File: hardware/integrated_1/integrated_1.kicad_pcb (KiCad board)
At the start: 2 copper layers, 37 parts, among them J1 USB4105-GF-A-120, U1 XC6SLX9-TQG144, U2 MAX17620ATA, U5 RP2040

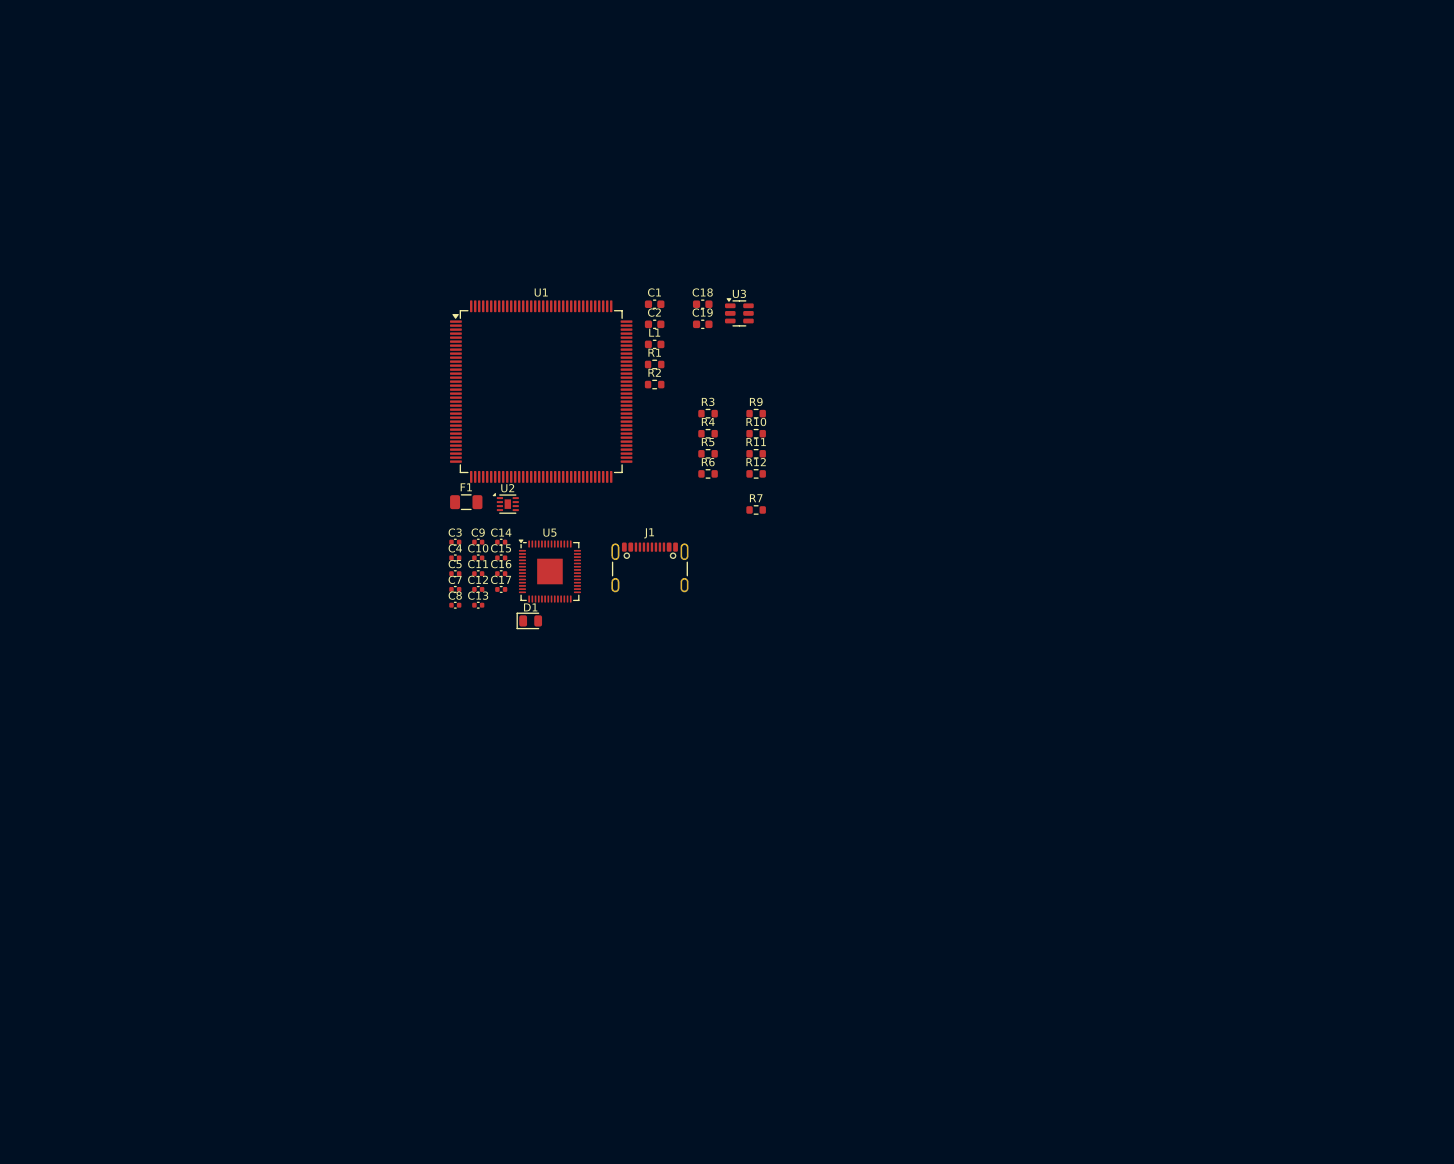
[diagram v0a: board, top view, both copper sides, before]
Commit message: created a rudementary shape and added a few parts and tracks to visualize pcb
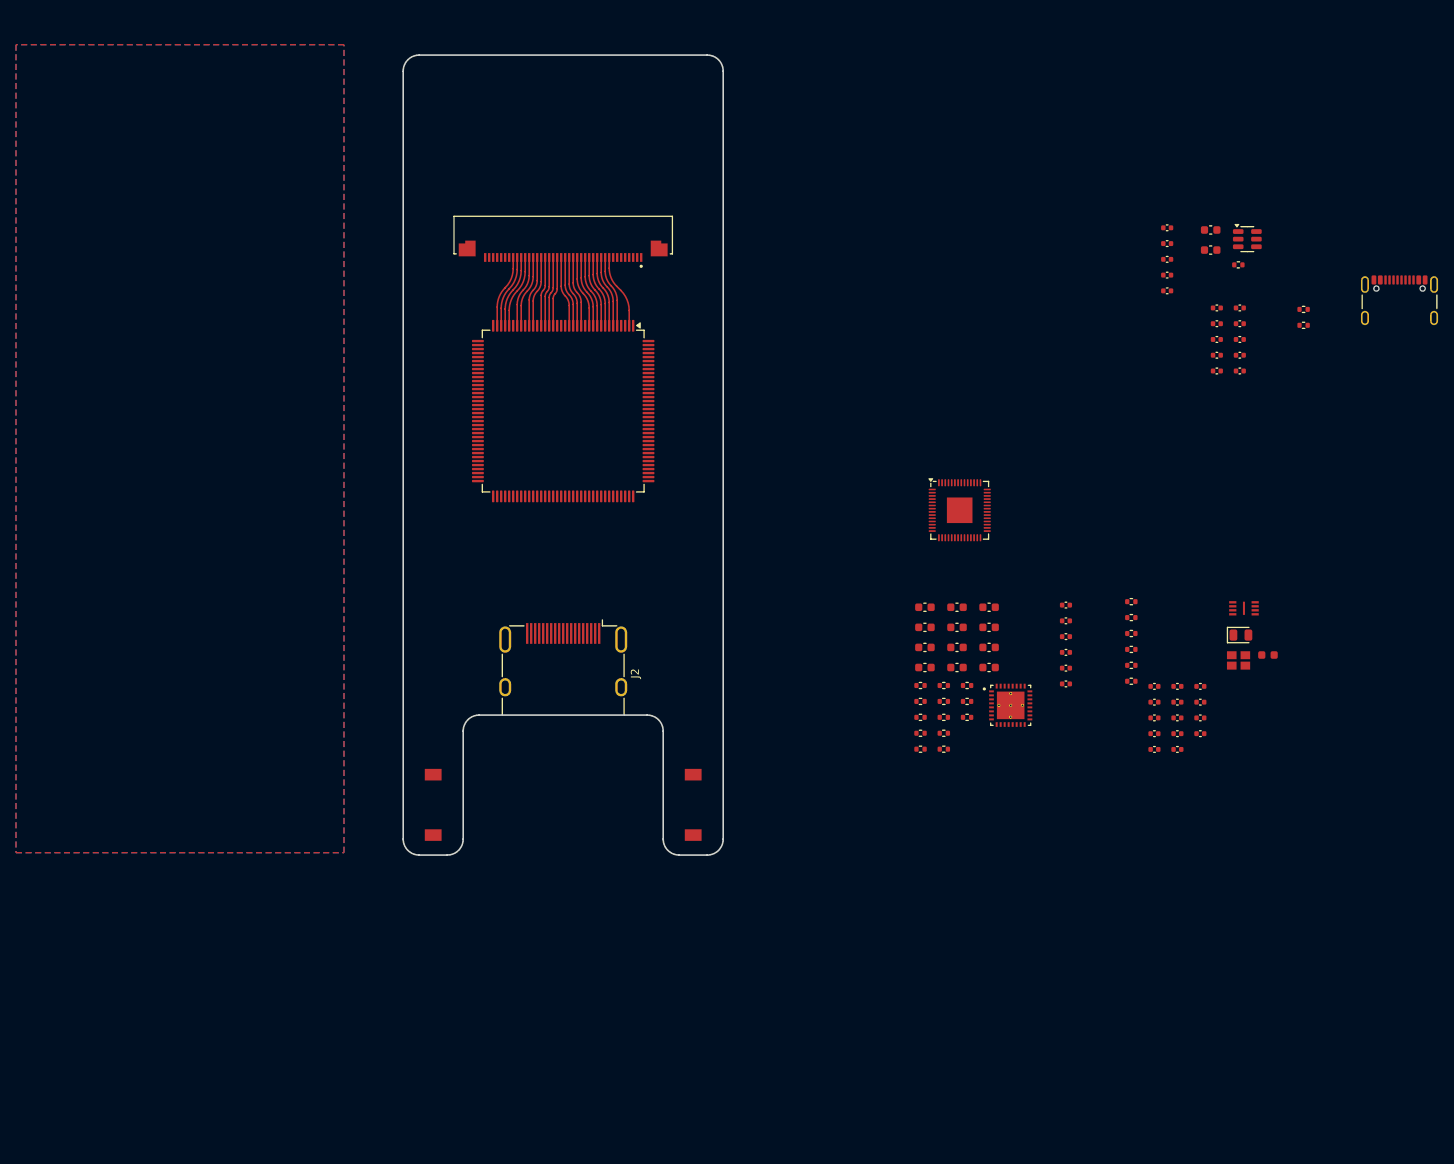
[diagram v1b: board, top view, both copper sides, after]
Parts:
- removed F1: 350mA, Fuse:Fuse_1206_3216Metric
- removed L1: 1u, Inductor_SMD:L_0603_1608Metric
- added C20: 100n, Capacitor_SMD:C_0402_1005Metric, F.Cu at (222.8, 128.4)
- added C21: 100n, Capacitor_SMD:C_0402_1005Metric, F.Cu at (222.8, 130.3)
- added C22: 100n, Capacitor_SMD:C_0402_1005Metric, F.Cu at (222.8, 132.3)
- added C23: 100n, Capacitor_SMD:C_0402_1005Metric, F.Cu at (225.6, 124.4)
- added C24: 100n, Capacitor_SMD:C_0402_1005Metric, F.Cu at (225.6, 126.4)
- added C25: 100n, Capacitor_SMD:C_0402_1005Metric, F.Cu at (225.6, 128.4)
- added C26: 1u, Capacitor_SMD:C_0402_1005Metric, F.Cu at (225.6, 130.3)
- added C27: 1u, Capacitor_SMD:C_0603_1608Metric, F.Cu at (226.9, 67.4)
- added C28: 1u, Capacitor_SMD:C_0603_1608Metric, F.Cu at (226.9, 69.9)
- added C29: 10u, Capacitor_SMD:C_0603_1608Metric, F.Cu at (191.2, 114.5)
- added C30: 1u, Capacitor_SMD:C_0603_1608Metric, F.Cu at (191.2, 117.0)
- added C31: 10u, Capacitor_SMD:C_0603_1608Metric, F.Cu at (191.2, 119.5)
- added C32: 10u, Capacitor_SMD:C_0603_1608Metric, F.Cu at (191.2, 122.1)
- added C35: 2u2, Capacitor_SMD:C_0603_1608Metric, F.Cu at (195.2, 114.5)
- added C36: 10u, Capacitor_SMD:C_0603_1608Metric, F.Cu at (195.2, 117.0)
- added C37: 10u, Capacitor_SMD:C_0603_1608Metric, F.Cu at (195.2, 119.5)
- added C38: 2u2, Capacitor_SMD:C_0603_1608Metric, F.Cu at (195.2, 122.1)
- added C39: 10u, Capacitor_SMD:C_0603_1608Metric, F.Cu at (199.2, 114.5)
- added C40: 10u, Capacitor_SMD:C_0603_1608Metric, F.Cu at (199.2, 117.0)
- added C41: 10u, Capacitor_SMD:C_0603_1608Metric, F.Cu at (199.2, 119.5)
- added C42: 10u, Capacitor_SMD:C_0603_1608Metric, F.Cu at (199.2, 122.1)
- added C54: 100n, Capacitor_SMD:C_0402_1005Metric, F.Cu at (227.7, 77.1)
- added C55: 100n, Capacitor_SMD:C_0402_1005Metric, F.Cu at (227.7, 79.1)
- added C56: 100n, Capacitor_SMD:C_0402_1005Metric, F.Cu at (227.7, 81.0)
- added C57: 100n, Capacitor_SMD:C_0402_1005Metric, F.Cu at (227.7, 83.0)
- added C58: 100n, Capacitor_SMD:C_0402_1005Metric, F.Cu at (227.7, 85.0)
- added C59: 100n, Capacitor_SMD:C_0402_1005Metric, F.Cu at (230.6, 77.1)
- added C6: 100n, Capacitor_SMD:C_0402_1005Metric, F.Cu at (208.8, 124.1)
- added C60: 100n, Capacitor_SMD:C_0402_1005Metric, F.Cu at (230.6, 79.1)
- added C61: 100n, Capacitor_SMD:C_0402_1005Metric, F.Cu at (230.6, 81.0)
- added C62: 100n, Capacitor_SMD:C_0402_1005Metric, F.Cu at (230.6, 83.0)
- added C63: 100n, Capacitor_SMD:C_0402_1005Metric, F.Cu at (230.6, 85.0)
- added DS1: ST7701_IPS_3.99_TOUCH, KiCAD Library:AMPHENOL_F32Q-1A7H1-11040, F.Cu at (146.0, 68.0)
- added J2: HDMI_A_1.4, Connector_HDMI:HDMI_A_Molex_208658-1001_Horizontal, F.Cu at (146.0, 121.1)
- added R13: 470k, Resistor_SMD:R_0402_1005Metric, F.Cu at (190.7, 130.3)
- added R14: 470k, Resistor_SMD:R_0402_1005Metric, F.Cu at (190.7, 132.3)
- added R15: 470k, Resistor_SMD:R_0402_1005Metric, F.Cu at (193.6, 124.3)
- added R16: 105k, Resistor_SMD:R_0402_1005Metric, F.Cu at (193.6, 126.3)
- added R17: 150k, Resistor_SMD:R_0402_1005Metric, F.Cu at (193.6, 128.3)
- added R18: 100k, Resistor_SMD:R_0402_1005Metric, F.Cu at (193.6, 130.3)
- added R19: 470k, Resistor_SMD:R_0402_1005Metric, F.Cu at (193.6, 132.3)
- added R20: 105k, Resistor_SMD:R_0402_1005Metric, F.Cu at (196.5, 124.3)
- added R21: 470k, Resistor_SMD:R_0402_1005Metric, F.Cu at (196.5, 126.3)
- added R22: 470k, Resistor_SMD:R_0402_1005Metric, F.Cu at (196.5, 128.3)
- added R8: 270, Resistor_SMD:R_0402_1005Metric, F.Cu at (217.0, 123.8)
- added SW1: DNF, KiCAD Library:PTS636 SM25J SMTR LFS, F.Cu at (129.8, 139.2)
- added SW2: DNF, KiCAD Library:PTS636 SM25J SMTR LFS, F.Cu at (162.2, 139.2)
- added U4: ~, Package_TO_SOT_SMD:SOT-23-6, F.Cu at (231.5, 68.5)
- added Y1: 12MHz, KiCAD Library:ECS120836CKMTR3, F.Cu at (230.4, 121.2)
- C1, C2: value 10u -> 100n; footprint Capacitor_SMD:C_0603_1608Metric -> Capacitor_SMD:C_0402_1005Metric
- C12, C13: value 100n -> 8p
- C15: value 100n -> 2u2; footprint Capacitor_SMD:C_0402_1005Metric -> KiCAD Library:C_0603_1608Metric
- C17, C9: value 1u -> 100n
- C18: footprint Capacitor_SMD:C_0603_1608Metric -> Capacitor_SMD:C_0402_1005Metric
- C19: value 1u -> 100n; footprint Capacitor_SMD:C_0603_1608Metric -> Capacitor_SMD:C_0402_1005Metric
- C3, C4: value 8p -> 100n
- R1: value 470k -> 5k1; footprint Resistor_SMD:R_0603_1608Metric -> Resistor_SMD:R_0402_1005Metric
- R10: value DNF -> 1k; footprint Resistor_SMD:R_0603_1608Metric -> Resistor_SMD:R_0402_1005Metric
- R11: value 1k -> 1R; footprint Resistor_SMD:R_0603_1608Metric -> Resistor_SMD:R_0402_1005Metric
- R12: value 270 -> 100k; footprint Resistor_SMD:R_0603_1608Metric -> Resistor_SMD:R_0402_1005Metric
- R2: value 150k -> 5k1; footprint Resistor_SMD:R_0603_1608Metric -> Resistor_SMD:R_0402_1005Metric
- R3: value 5k1 -> 10K; footprint Resistor_SMD:R_0603_1608Metric -> Resistor_SMD:R_0402_1005Metric
- R4: value 5k1 -> DNF; footprint Resistor_SMD:R_0603_1608Metric -> Resistor_SMD:R_0402_1005Metric
- R5: value 27 -> 1k; footprint Resistor_SMD:R_0603_1608Metric -> Resistor_SMD:R_0402_1005Metric
- R6: footprint Resistor_SMD:R_0603_1608Metric -> Resistor_SMD:R_0402_1005Metric
- R7: value 12R5 -> 27; footprint Resistor_SMD:R_0603_1608Metric -> Resistor_SMD:R_0402_1005Metric
- R9: value 10K -> 12R5; footprint Resistor_SMD:R_0603_1608Metric -> Resistor_SMD:R_0402_1005Metric
- U2: value MAX17620ATA -> W25Q16JV; footprint Package_DFN_QFN:TDFN-8-1EP_2x2mm_P0.5mm_EP0.8x1.2mm -> KiCAD Library:W25Q16JVUXIQ TR
- U3: value ~ -> RP2040; footprint Package_TO_SOT_SMD:SOT-23-6 -> Package_DFN_QFN:QFN-56-1EP_7x7mm_P0.4mm_EP3.2x3.2mm
- U5: value RP2040 -> TPS650250RHBR; footprint Package_DFN_QFN:QFN-56-1EP_7x7mm_P0.4mm_EP3.2x3.2mm -> KiCAD Library:IC_ADS125H01IRHBT
- moved C7 99.8 mm to (221.5, 67.1)
- moved C8 99.8 mm to (221.5, 69.1)
- moved J1 99.5 mm to (250.5, 77.3)
- moved C15 96.6 mm to (234.1, 120.5)
- moved C10 93.1 mm to (221.5, 73.0)
- moved C11 93.1 mm to (221.5, 75.0)
- moved C9 93.1 mm to (221.5, 71.0)
- moved U2 92.9 mm to (231.1, 114.7)
- moved D1 88.8 mm to (230.7, 118.0)
- moved C12 85.4 mm to (219.9, 124.4)
- moved C13 85.4 mm to (219.9, 126.4)
- moved C14 84.6 mm to (219.9, 128.4)
- moved C16 84.1 mm to (219.9, 130.3)
- moved C17 84.1 mm to (219.9, 132.3)
- moved R2 81.5 mm to (238.6, 79.3)
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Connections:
- C1 pad 1: /FPGA Power/IN -> +3V3
- C12 pad 1: +3V3 -> GND
- C12 pad 2: GND -> /RP2040/XIN
- C13 pad 1: +3V3 -> GND
- C13 pad 2: GND -> /RP2040/XOUT_R
- C16 pad 1: +3V3 -> /RP2040/1V1
- C17 pad 1: +3V3 -> /RP2040/1V1
- C18 pad 1: +5V -> /RP2040/1V1
- C19 pad 1: /LEDA -> +3V3
- C3 pad 1: GND -> +3V3
- C3 pad 2: /RP2040/XIN -> GND
- C4 pad 1: GND -> +3V3
- C4 pad 2: /RP2040/XOUT_R -> GND
- C7 pad 1: /RP2040/1V1 -> +3V3
- C8 pad 1: /RP2040/1V1 -> +3V3
- C9 pad 1: /RP2040/1V1 -> +3V3
- J1 pad A6: /D+ -> /USB_D+
- J1 pad A7: /D- -> /USB_D-
- J1 pad B6: /D+ -> /USB_D+
- J1 pad B7: /D- -> /USB_D-
- R1 pad 1: +3V3 -> Net-(J1-CC2)
- R1 pad 2: /FPGA Power/FB -> GND
- R10 pad 1: /RP2040/QSPI_SS -> +5V
- R10 pad 2: +3V3 -> /Buck Converter/EN
- R11 pad 1: /RP2040/XOUT -> +5V
- R11 pad 2: /RP2040/XOUT_R -> Net-(U5-VCC)
- R12 pad 1: Net-(D1-A) -> +3V3
- R12 pad 2: /RP2040/LED_STATUS -> /Buck Converter/~{PWR_FAIL}
- R2 pad 1: /FPGA Power/FB -> Net-(J1-CC1)
- R3 pad 1: Net-(J1-CC2) -> /RP2040/QSPI_SS
- R3 pad 2: GND -> Net-(R3-Pad2)
- R4 pad 1: Net-(J1-CC1) -> /RP2040/QSPI_SS
- R4 pad 2: GND -> +3V3
- R5 pad 1: /D- -> /RP2040/XOUT
- R5 pad 2: /USB_D- -> /RP2040/XOUT_R
- R6 pad 1: /D+ -> /USB_D+
- R6 pad 2: /USB_D+ -> /RP2040/D+
- R7 pad 1: /LEDK -> /USB_D-
- R7 pad 2: GND -> /RP2040/D-
- R9 pad 1: /RP2040/QSPI_SS -> /LEDK
- R9 pad 2: Net-(R9-Pad2) -> GND
- U1 pad 1: unconnected-(U1B-IO_L83N_VREF_3-Pad1) -> /~{RST}
- U1 pad 10: unconnected-(U1B-IO_L50P_3-Pad10) -> /HS
- U1 pad 103: unconnected-(U1A-VCCO_1-Pad103) -> +3V3
- U1 pad 11: unconnected-(U1B-IO_L49N_3-Pad11) -> /DB0
- U1 pad 111: unconnected-(U1A-IO_L66N_SCP0_0-Pad111) -> /FPGA_D7
- U1 pad 112: unconnected-(U1A-IO_L66P_SCP1_0-Pad112) -> /FPGA_D6
- U1 pad 114: unconnected-(U1A-IO_L65N_SCP2_0-Pad114) -> /FPGA_D5
- U1 pad 115: unconnected-(U1A-IO_L65P_SCP3_0-Pad115) -> /FPGA_D4
- U1 pad 116: unconnected-(U1A-IO_L64N_SCP4_0-Pad116) -> /FPGA_D3
- U1 pad 117: unconnected-(U1A-IO_L64P_SCP5_0-Pad117) -> /FPGA_D2
- U1 pad 118: unconnected-(U1A-IO_L63N_SCP6_0-Pad118) -> /FPGA_D1
- U1 pad 119: unconnected-(U1A-IO_L63P_SCP7_0-Pad119) -> /FPGA_D0
- U1 pad 12: unconnected-(U1B-IO_L49P_3-Pad12) -> /DB1
- U1 pad 120: unconnected-(U1A-IO_L62N_VREF_0-Pad120) -> /FPGA_RD
- U1 pad 121: unconnected-(U1A-IO_L62P_0-Pad121) -> /FPGA_CLK
- U1 pad 122: unconnected-(U1A-VCCO_0-Pad122) -> +3V3
- U1 pad 123: unconnected-(U1A-IO_L37N_GCLK12_0-Pad123) -> /FPGA_WR
- U1 pad 124: unconnected-(U1A-IO_L37P_GCLK13_0-Pad124) -> /FPGA IO Bank A/CLK_{50}
- U1 pad 125: unconnected-(U1A-VCCO_0-Pad125) -> +3V3
- U1 pad 127: unconnected-(U1A-IO_L36P_GCLK15_0-Pad127) -> /DVI_UTIL
- U1 pad 128: 1V2 -> /VCC_{AUX}
- U1 pad 129: +3V3 -> /VCC_{AUX}
- U1 pad 131: unconnected-(U1A-IO_L35N_GCLK16_0-Pad131) -> /DVI_HPD
- U1 pad 132: unconnected-(U1A-IO_L35P_GCLK17_0-Pad132) -> /DVI_SDA
- U1 pad 133: unconnected-(U1A-IO_L34N_GCLK18_0-Pad133) -> /DVI_SCL
- U1 pad 134: unconnected-(U1A-IO_L34P_GCLK19_0-Pad134) -> /DVI_CEC
- U1 pad 135: unconnected-(U1A-VCCO_0-Pad135) -> +3V3
- U1 pad 137: unconnected-(U1A-IO_L4N_0-Pad137) -> /DVI_CK-
- U1 pad 138: unconnected-(U1A-IO_L4P_0-Pad138) -> /DVI_CK+
- U1 pad 139: unconnected-(U1A-IO_L3N_0-Pad139) -> /DVI_D0-
- U1 pad 14: unconnected-(U1B-IO_L44N_GCLK20_3-Pad14) -> /DB2
- U1 pad 140: unconnected-(U1A-IO_L3P_0-Pad140) -> /DVI_D0+
- U1 pad 141: unconnected-(U1A-IO_L2N_0-Pad141) -> /DVI_D1-
- U1 pad 142: unconnected-(U1A-IO_L2P_0-Pad142) -> /DVI_D1+
- U1 pad 143: unconnected-(U1A-IO_L1N_VREF_0-Pad143) -> /DVI_D2-
- U1 pad 144: unconnected-(U1A-IO_L1P_HSWAPEN_0-Pad144) -> /DVI_D2+
- U1 pad 15: unconnected-(U1B-IO_L44P_GCLK21_3-Pad15) -> /DB3
- U1 pad 16: unconnected-(U1B-IO_L43N_GCLK22_IRDY2_3-Pad16) -> /DB4
- U1 pad 17: unconnected-(U1B-IO_L43P_GCLK23_3-Pad17) -> /DB5
- U1 pad 18: unconnected-(U1B-VCCO_3-Pad18) -> +3V3
- U1 pad 19: 1V2 -> /VCC_{AUX}
- U1 pad 2: unconnected-(U1B-IO_L83P_3-Pad2) -> /SDA
- U1 pad 20: +3V3 -> /VCC_{AUX}
- U1 pad 21: unconnected-(U1B-IO_L42N_GCLK24_3-Pad21) -> /DB6
- U1 pad 22: unconnected-(U1B-IO_L42P_GCLK25_TRDY2_3-Pad22) -> /DB7
- U1 pad 23: unconnected-(U1B-IO_L41N_GCLK26_3-Pad23) -> /DB8
- U1 pad 24: unconnected-(U1B-IO_L41P_GCLK27_3-Pad24) -> /DB9
- U1 pad 26: unconnected-(U1B-IO_L37N_3-Pad26) -> /DB10
- U1 pad 27: unconnected-(U1B-IO_L37P_3-Pad27) -> /DB11
- U1 pad 28: 1V2 -> /VCC_{AUX}
- U1 pad 29: unconnected-(U1B-IO_L36N_3-Pad29) -> /DB12
- U1 pad 30: unconnected-(U1B-IO_L36P_3-Pad30) -> /DB13
- U1 pad 31: unconnected-(U1B-VCCO_3-Pad31) -> +3V3
- U1 pad 32: unconnected-(U1B-IO_L2N_3-Pad32) -> /DB14
- U1 pad 33: unconnected-(U1B-IO_L2P_3-Pad33) -> /DB15
- U1 pad 34: unconnected-(U1B-IO_L1N_VREF_3-Pad34) -> /DB16
- U1 pad 35: unconnected-(U1B-IO_L1P_3-Pad35) -> /DB17
- U1 pad 36: +3V3 -> /VCC_{AUX}
- U1 pad 4: unconnected-(U1B-VCCO_3-Pad4) -> +3V3
- U1 pad 42: unconnected-(U1B-VCCO_2-Pad42) -> +3V3
- U1 pad 5: unconnected-(U1B-IO_L52N_3-Pad5) -> /SCL
- U1 pad 52: 1V2 -> /VCC_{AUX}
- U1 pad 53: +3V3 -> /VCC_{AUX}
- U1 pad 6: unconnected-(U1B-IO_L52P_3-Pad6) -> /CS
- U1 pad 63: unconnected-(U1B-VCCO_2-Pad63) -> +3V3
- U1 pad 7: unconnected-(U1B-IO_L51N_3-Pad7) -> /DCLK
- U1 pad 76: unconnected-(U1A-VCCO_1-Pad76) -> +3V3
- U1 pad 8: unconnected-(U1B-IO_L51P_3-Pad8) -> /DE
- U1 pad 86: unconnected-(U1A-VCCO_1-Pad86) -> +3V3
- U1 pad 89: 1V2 -> /VCC_{AUX}
- U1 pad 9: unconnected-(U1B-IO_L50N_3-Pad9) -> /VS
- U1 pad 90: +3V3 -> /VCC_{AUX}
- U2 pad 1: /FPGA Power/IN -> /RP2040/QSPI_SS
- U2 pad 2: GND -> /RP2040/QSPI_SD1
- U2 pad 3: /FPGA Power/IN -> /RP2040/QSPI_SD2
- U2 pad 4: unconnected-(U2-MODE-Pad4) -> GND
- U2 pad 5: unconnected-(U2-PGOOD-Pad5) -> /RP2040/QSPI_SD0
- U2 pad 6: /FPGA Power/FB -> /RP2040/QSPI_SCLK
- U2 pad 7: +3V3 -> /RP2040/QSPI_SD3
- U2 pad 8: /FPGA Power/LX -> +3V3
- U2 pad 9: GND -> (no net)
- U3 pad 1: Net-(D2-A) -> +3V3
- U3 pad 2: GND -> /RP2040/DEBUG_UART_TX
- U3 pad 3: /LEDK -> /RP2040/DEBUG_UART_RX
- U3 pad 4: /Backlight/BL_PWM -> /BL_PWM
- U3 pad 5: /LEDA -> /FPGA_WR
- U3 pad 6: +5V -> /FPGA_RD
- U5 pad 10: +3V3 -> +1V8
- U5 pad 11: /FPGA_D2 -> /Buck Converter/FB_{LDO1}
- U5 pad 12: /FPGA_D3 -> unconnected-(U5-VDD_ALIVE-Pad12)
- U5 pad 13: /FPGA_D4 -> GND
- U5 pad 14: /FPGA_D5 -> +1V8
- U5 pad 15: /FPGA_D6 -> +5V
- U5 pad 16: /FPGA_D7 -> +2V5
- U5 pad 17: unconnected-(U5-GPIO14-Pad17) -> /Buck Converter/EN
- U5 pad 18: unconnected-(U5-GPIO15-Pad18) -> /Buck Converter/EN
- U5 pad 19: unconnected-(U5-TESTEN-Pad19) -> /Buck Converter/EN
- U5 pad 2: /RP2040/DEBUG_UART_TX -> GND
- U5 pad 20: /RP2040/XIN -> /Buck Converter/EN
- U5 pad 21: /RP2040/XOUT -> /Buck Converter/~{PWR_FAIL}
- U5 pad 22: +3V3 -> /Buck Converter/FB_{DCDC_{2}}
- U5 pad 23: /RP2040/1V1 -> unconnected-(U5-MODE-Pad23)
- U5 pad 24: /RP2040/SWCLK -> GND
- U5 pad 25: /RP2040/SWD -> /VCC_{AUX}
- U5 pad 26: Net-(U5-RUN) -> GND
- U5 pad 27: /TDI -> Net-(U5-L2)
- U5 pad 28: /TDO -> +5V
- U5 pad 29: /TCK -> Net-(U5-VCC)
- U5 pad 3: /RP2040/DEBUG_UART_RX -> Net-(U5-L3)
- U5 pad 30: /TMS -> unconnected-(U5-PWRFAIL_SNS-Pad30)
- U5 pad 31: /TP_SDA -> GND
- U5 pad 32: /TP_SCL -> /Buck Converter/FB_{DCDC_{3}}
- U5 pad 33: +3V3 -> GND
- U5 pad 34: /TP_RST -> (no net)
- U5 pad 35: /TP_INT -> (no net)
- U5 pad 36: unconnected-(U5-GPIO24-Pad36) -> (no net)
- U5 pad 37: /RP2040/LED_STATUS -> (no net)
- U5 pad 38: unconnected-(U5-GPIO26_ADC0-Pad38) -> (no net)
- U5 pad 4: unconnected-(U5-GPIO2-Pad4) -> +5V
- U5 pad 5: /FPGA_WR -> +5V
- U5 pad 6: /FPGA_RD -> Net-(U5-L1)
- U5 pad 7: /FPGA_CLK -> GND
- U5 pad 8: /FPGA_D0 -> /VCC_{AUX}
- U5 pad 9: /FPGA_D1 -> Net-(U5-DEFDCDC1)
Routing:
- net /SDA: track 0.00 -> 9.25 mm
- net /DB15: track 0.00 -> 9.10 mm
- net /DB17: track 0.00 -> 9.04 mm
- net /DB14: track 0.00 -> 9.04 mm
- net /DB16: track 0.00 -> 9.04 mm
- net /DB12: track 0.00 -> 8.91 mm
- net /DE: track 0.00 -> 8.91 mm
- net /DB1: track 0.00 -> 8.91 mm
- net /HS: track 0.00 -> 8.91 mm
- net /DCLK: track 0.00 -> 8.91 mm
- net /DB13: track 0.00 -> 8.91 mm
- net /VS: track 0.00 -> 8.91 mm
- net /CS: track 0.00 -> 8.91 mm
- net /SCL: track 0.00 -> 8.91 mm
- net /DB0: track 0.00 -> 8.91 mm
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- added copper zone on B.Cu, net GND
- added copper zone on F.Cu, net GND
- added copper zone on In1.Cu, net GND
- added copper zone on In2.Cu, net GND
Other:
- board outline added: 40 x 100 mm
- copper layers 2 -> 4

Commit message: rearranged the pinout to make more sense
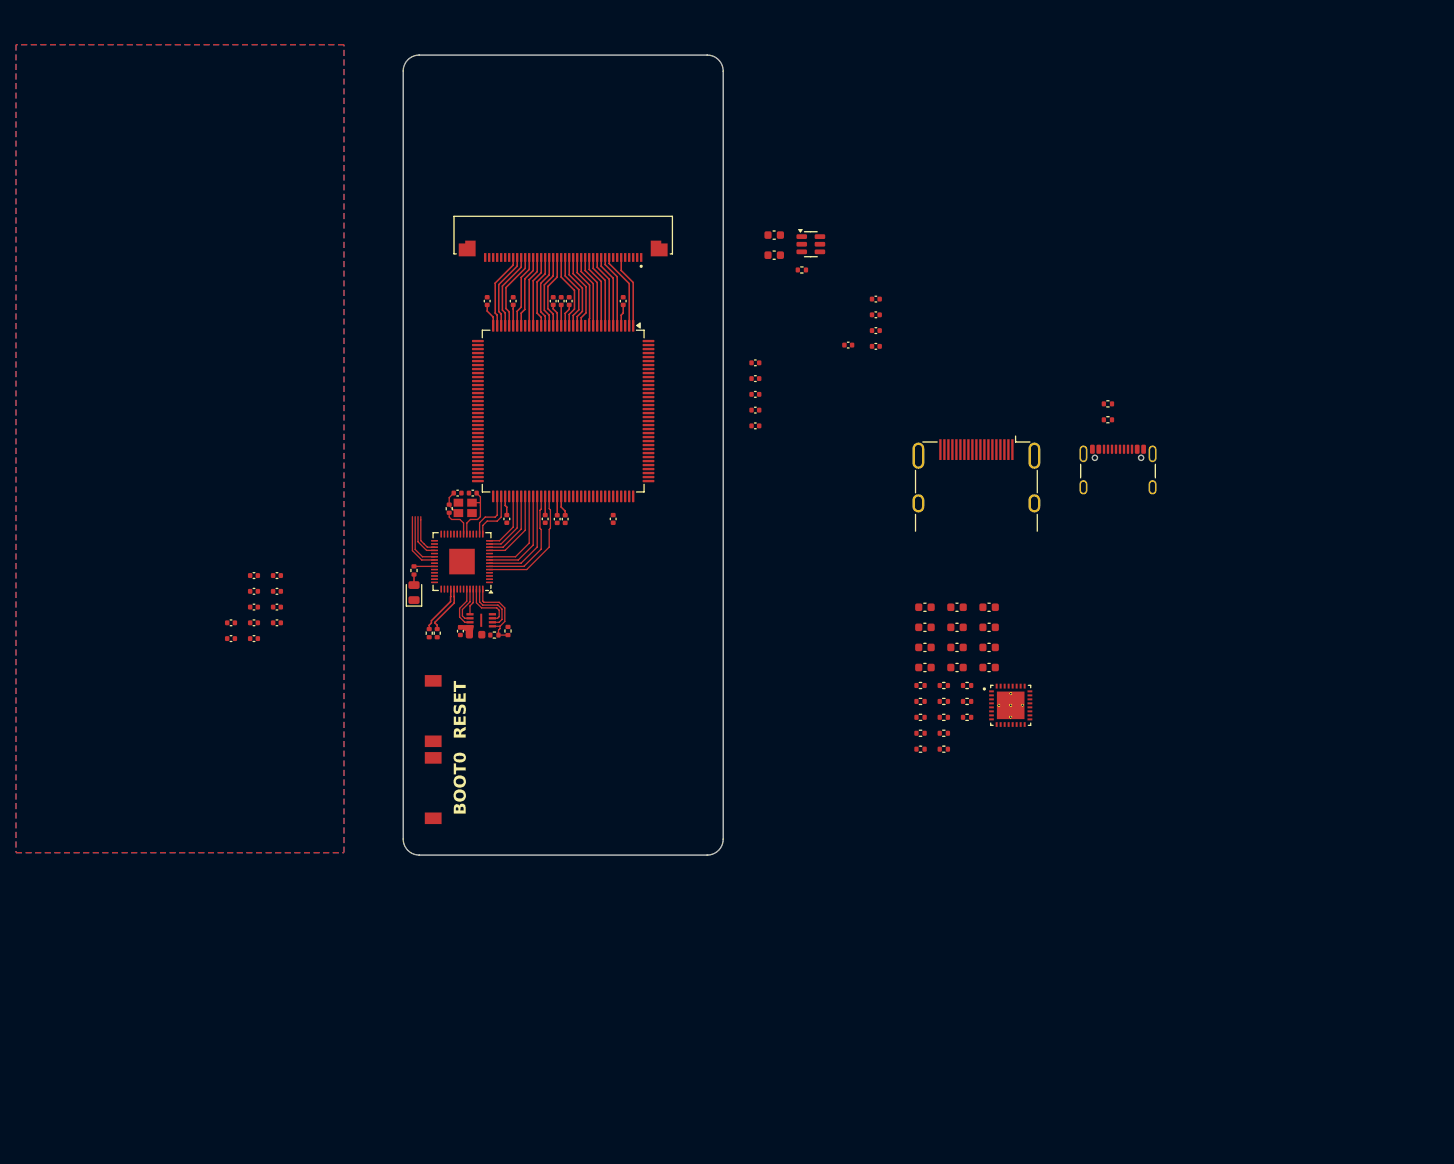
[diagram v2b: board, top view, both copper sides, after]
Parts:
- moved C16 116.3 mm to (104.5, 116.5)
- moved C17 116.3 mm to (104.5, 118.4)
- moved C18 116.3 mm to (107.3, 110.6)
- moved C19 116.3 mm to (107.3, 112.5)
- moved C20 116.3 mm to (107.3, 114.5)
- moved C21 116.3 mm to (107.3, 116.5)
- moved C22 116.3 mm to (107.3, 118.4)
- moved C23 116.3 mm to (110.2, 110.6)
- moved C24 116.3 mm to (110.2, 112.5)
- moved C25 116.3 mm to (110.2, 114.5)
- moved C26 116.3 mm to (110.2, 116.5)
- moved D1 103.5 mm to (127.3, 112.7), turned to 90 degrees
- moved C15 99.1 mm to (135.1, 118.0)
- moved Y1 98.5 mm to (133.8, 102.1), turned to 180 degrees
- moved U2 95.4 mm to (135.8, 116.2), turned to 180 degrees
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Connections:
- net /FPGA IO Bank A/CLK_{50} renamed /FPGA IO Bank A/GPIO1_14
- U1 pad 100: unconnected-(U1A-IO_L33P_1-Pad100) -> /DVI_D0+
- U1 pad 101: unconnected-(U1A-IO_L32N_1-Pad101) -> /DVI_D1-
- U1 pad 102: unconnected-(U1A-IO_L32P_1-Pad102) -> /DVI_D1+
- U1 pad 104: unconnected-(U1A-IO_L1N_VREF_1-Pad104) -> /DVI_D2-
- U1 pad 105: unconnected-(U1A-IO_L1P_1-Pad105) -> /DVI_D2+
- U1 pad 111: /FPGA_D7 -> /FPGA IO Bank A/GPIO1_25
- U1 pad 112: /FPGA_D6 -> /FPGA IO Bank A/GPIO1_24
- U1 pad 114: /FPGA_D5 -> /FPGA IO Bank A/GPIO1_23
- U1 pad 115: /FPGA_D4 -> /FPGA IO Bank A/GPIO1_22
- U1 pad 116: /FPGA_D3 -> /FPGA IO Bank A/GPIO1_21
- U1 pad 117: /FPGA_D2 -> /FPGA IO Bank A/GPIO1_20
- U1 pad 118: /FPGA_D1 -> /FPGA IO Bank A/GPIO1_19
- U1 pad 119: /FPGA_D0 -> /FPGA IO Bank A/GPIO1_18
- U1 pad 120: /FPGA_RD -> /FPGA IO Bank A/GPIO1_17
- U1 pad 121: /FPGA_CLK -> /FPGA IO Bank A/GPIO1_16
- U1 pad 123: /FPGA_WR -> /FPGA IO Bank A/GPIO1_15
- U1 pad 126: unconnected-(U1A-IO_L36N_GCLK14_0-Pad126) -> /FPGA IO Bank A/GPIO1_13
- U1 pad 127: /DVI_UTIL -> /FPGA IO Bank A/GPIO1_12
- U1 pad 131: /DVI_HPD -> /FPGA IO Bank A/GPIO1_11
- U1 pad 132: /DVI_SDA -> /FPGA IO Bank A/GPIO1_10
- U1 pad 133: /DVI_SCL -> /FPGA IO Bank A/GPIO1_09
- U1 pad 134: /DVI_CEC -> /FPGA IO Bank A/GPIO1_08
- U1 pad 137: /DVI_CK- -> /FPGA IO Bank A/GPIO1_07
- U1 pad 138: /DVI_CK+ -> /FPGA IO Bank A/GPIO1_06
- U1 pad 139: /DVI_D0- -> /FPGA IO Bank A/GPIO1_05
- U1 pad 140: /DVI_D0+ -> /FPGA IO Bank A/GPIO1_04
- U1 pad 141: /DVI_D1- -> /FPGA IO Bank A/GPIO1_03
- U1 pad 142: /DVI_D1+ -> /FPGA IO Bank A/GPIO1_02
- U1 pad 143: /DVI_D2- -> /FPGA IO Bank A/GPIO1_01
- U1 pad 144: /DVI_D2+ -> /FPGA IO Bank A/GPIO1_00
- U1 pad 38: unconnected-(U1B-IO_L65N_CSO_B_2-Pad38) -> /FPGA IO Bank B/GPIO0_25
- U1 pad 39: unconnected-(U1B-IO_L65P_INIT_B_2-Pad39) -> /FPGA IO Bank B/GPIO0_24
- U1 pad 40: unconnected-(U1B-IO_L64N_D9_2-Pad40) -> /FPGA IO Bank B/GPIO0_23
- U1 pad 41: unconnected-(U1B-IO_L64P_D8_2-Pad41) -> /FPGA IO Bank B/GPIO0_22
- U1 pad 43: unconnected-(U1B-IO_L62N_D6_2-Pad43) -> /FPGA IO Bank B/GPIO0_21
- U1 pad 44: unconnected-(U1B-IO_L62P_D5_2-Pad44) -> /FPGA IO Bank B/GPIO0_20
- U1 pad 45: unconnected-(U1B-IO_L49N_D4_2-Pad45) -> /FPGA IO Bank B/GPIO0_19
- U1 pad 46: unconnected-(U1B-IO_L49P_D3_2-Pad46) -> /FPGA IO Bank B/GPIO0_18
- U1 pad 47: unconnected-(U1B-IO_L48N_RDWR_B_VREF_2-Pad47) -> /FPGA IO Bank B/GPIO0_17
- U1 pad 48: unconnected-(U1B-IO_L48P_D7_2-Pad48) -> /FPGA IO Bank B/GPIO0_16
- U1 pad 50: unconnected-(U1B-IO_L31N_GCLK30_D15_2-Pad50) -> /FPGA IO Bank B/GPIO0_15
- U1 pad 51: unconnected-(U1B-IO_L31P_GCLK31_D14_2-Pad51) -> /FPGA IO Bank B/GPIO0_14
- U1 pad 55: unconnected-(U1B-IO_L30N_GCLK0_USERCCLK_2-Pad55) -> /FPGA IO Bank B/GPIO0_13
- U1 pad 56: unconnected-(U1B-IO_L30P_GCLK1_D13_2-Pad56) -> /FPGA IO Bank B/GPIO0_12
- U1 pad 57: unconnected-(U1B-IO_L14N_D12_2-Pad57) -> /FPGA IO Bank B/GPIO0_11
- U1 pad 58: unconnected-(U1B-IO_L14P_D11_2-Pad58) -> /FPGA IO Bank B/GPIO0_10
- U1 pad 59: unconnected-(U1B-IO_L13N_D10_2-Pad59) -> /FPGA IO Bank B/GPIO0_09
- U1 pad 60: unconnected-(U1B-IO_L13P_M1_2-Pad60) -> /FPGA IO Bank B/GPIO0_08
- U1 pad 61: unconnected-(U1B-IO_L12N_D2_MISO3_2-Pad61) -> /FPGA IO Bank B/GPIO0_07
- U1 pad 62: unconnected-(U1B-IO_L12P_D1_MISO2_2-Pad62) -> /FPGA IO Bank B/GPIO0_06
- U1 pad 64: unconnected-(U1B-IO_L3N_MOSI_CSI_B_MISO0_2-Pad64) -> /FPGA IO Bank B/GPIO0_05
- U1 pad 65: unconnected-(U1B-IO_L3P_D0_DIN_MISO_MISO1_2-Pad65) -> /FPGA IO Bank B/GPIO0_04
- U1 pad 66: unconnected-(U1B-IO_L2N_CMPMOSI_2-Pad66) -> /FPGA IO Bank B/GPIO0_03
- U1 pad 67: unconnected-(U1B-IO_L2P_CMPCLK_2-Pad67) -> /FPGA IO Bank B/GPIO0_02
- U1 pad 69: unconnected-(U1B-IO_L1N_M0_CMPMISO_2-Pad69) -> /FPGA IO Bank B/GPIO0_01
- U1 pad 70: unconnected-(U1B-IO_L1P_CCLK_2-Pad70) -> /FPGA IO Bank B/GPIO0_00
- U1 pad 74: unconnected-(U1A-IO_L74N_DOUT_BUSY_1-Pad74) -> /FPGA_D7
- U1 pad 75: unconnected-(U1A-IO_L74P_AWAKE_1-Pad75) -> /FPGA_D6
- U1 pad 78: unconnected-(U1A-IO_L47N_1-Pad78) -> /FPGA_D5
- U1 pad 79: unconnected-(U1A-IO_L47P_1-Pad79) -> /FPGA_D4
- U1 pad 80: unconnected-(U1A-IO_L46N_1-Pad80) -> /FPGA_D3
- U1 pad 81: unconnected-(U1A-IO_L46P_1-Pad81) -> /FPGA_D2
- U1 pad 82: unconnected-(U1A-IO_L45N_1-Pad82) -> /FPGA_D1
- U1 pad 83: unconnected-(U1A-IO_L45P_1-Pad83) -> /FPGA_D0
- U1 pad 84: unconnected-(U1A-IO_L43N_GCLK4_1-Pad84) -> /FPGA_CLK
- U1 pad 85: unconnected-(U1A-IO_L43P_GCLK5_1-Pad85) -> /FPGA_RD
- U1 pad 87: unconnected-(U1A-IO_L42N_GCLK6_TRDY1_1-Pad87) -> /FPGA_WR
- U1 pad 88: unconnected-(U1A-IO_L42P_GCLK7_1-Pad88) -> /DVI_UTIL
- U1 pad 92: unconnected-(U1A-IO_L41N_GCLK8_1-Pad92) -> /DVI_HPD
- U1 pad 93: unconnected-(U1A-IO_L41P_GCLK9_IRDY1_1-Pad93) -> /DVI_SDA
- U1 pad 94: unconnected-(U1A-IO_L40N_GCLK10_1-Pad94) -> /DVI_SCL
- U1 pad 95: unconnected-(U1A-IO_L40P_GCLK11_1-Pad95) -> /DVI_CEC
- U1 pad 97: unconnected-(U1A-IO_L34N_1-Pad97) -> /DVI_CK-
- U1 pad 98: unconnected-(U1A-IO_L34P_1-Pad98) -> /DVI_CK+
- U1 pad 99: unconnected-(U1A-IO_L33N_1-Pad99) -> /DVI_D0-
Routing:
- net /FPGA_WR: track 0.00 -> 15.1 mm
- net /FPGA_RD: track 0.00 -> 14.1 mm
- net /VCC_{AUX}: track 0.00 -> 13.3 mm
- net /FPGA_CLK: track 0.00 -> 13.1 mm
- net +3V3: track 0.00 -> 12.9 mm
- net /FPGA_D0: track 0.00 -> 12.3 mm
- net /FPGA_D1: track 0.00 -> 11.5 mm
- net /RP2040/QSPI_SS: track 0.00 -> 10.5 mm
- net /FPGA_D2: track 0.00 -> 9.74 mm
- net /~{RST}: track 0.00 -> 9.16 mm
- net /FPGA_D3: track 0.00 -> 8.99 mm
- net /FPGA_D4: track 0.00 -> 8.23 mm
- net /RP2040/XIN: track 0.00 -> 7.60 mm
- net /FPGA_D5: track 0.00 -> 7.51 mm
- net /TP_INT: track 0.00 -> 7.49 mm
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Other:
- outline, holes or cut-outs redrawn
- board text added: "BOOT0"
- board text added: "RESET"
